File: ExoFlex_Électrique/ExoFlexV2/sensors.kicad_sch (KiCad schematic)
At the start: 38 parts, among them J10 Screw_Terminal_01x02, J11 Screw_Terminal_01x02, J12 Screw_Terminal_01x02, J13 Screw_Terminal_01x02, J14 Screw_Terminal_01x02, J15 Screw_Terminal_01x02, J16 Screw_Terminal_01x02, J17 Screw_Terminal_5V, J18 Screw_Terminal_01x02, J19 Screw_Terminal_GND, J8 Screw_Terminal_01x02, J9 Screw_Terminal_01x02, Q1 S8550, Q2 S8550, Q3 S8550, U10 Switch(5A), U11 Switch(5A), U12 Switch(5A), U5 HX711, U6 HX711, U7 HX711, U8 MPU6050_acc_gyro, U9 MPU6050_acc_gyro

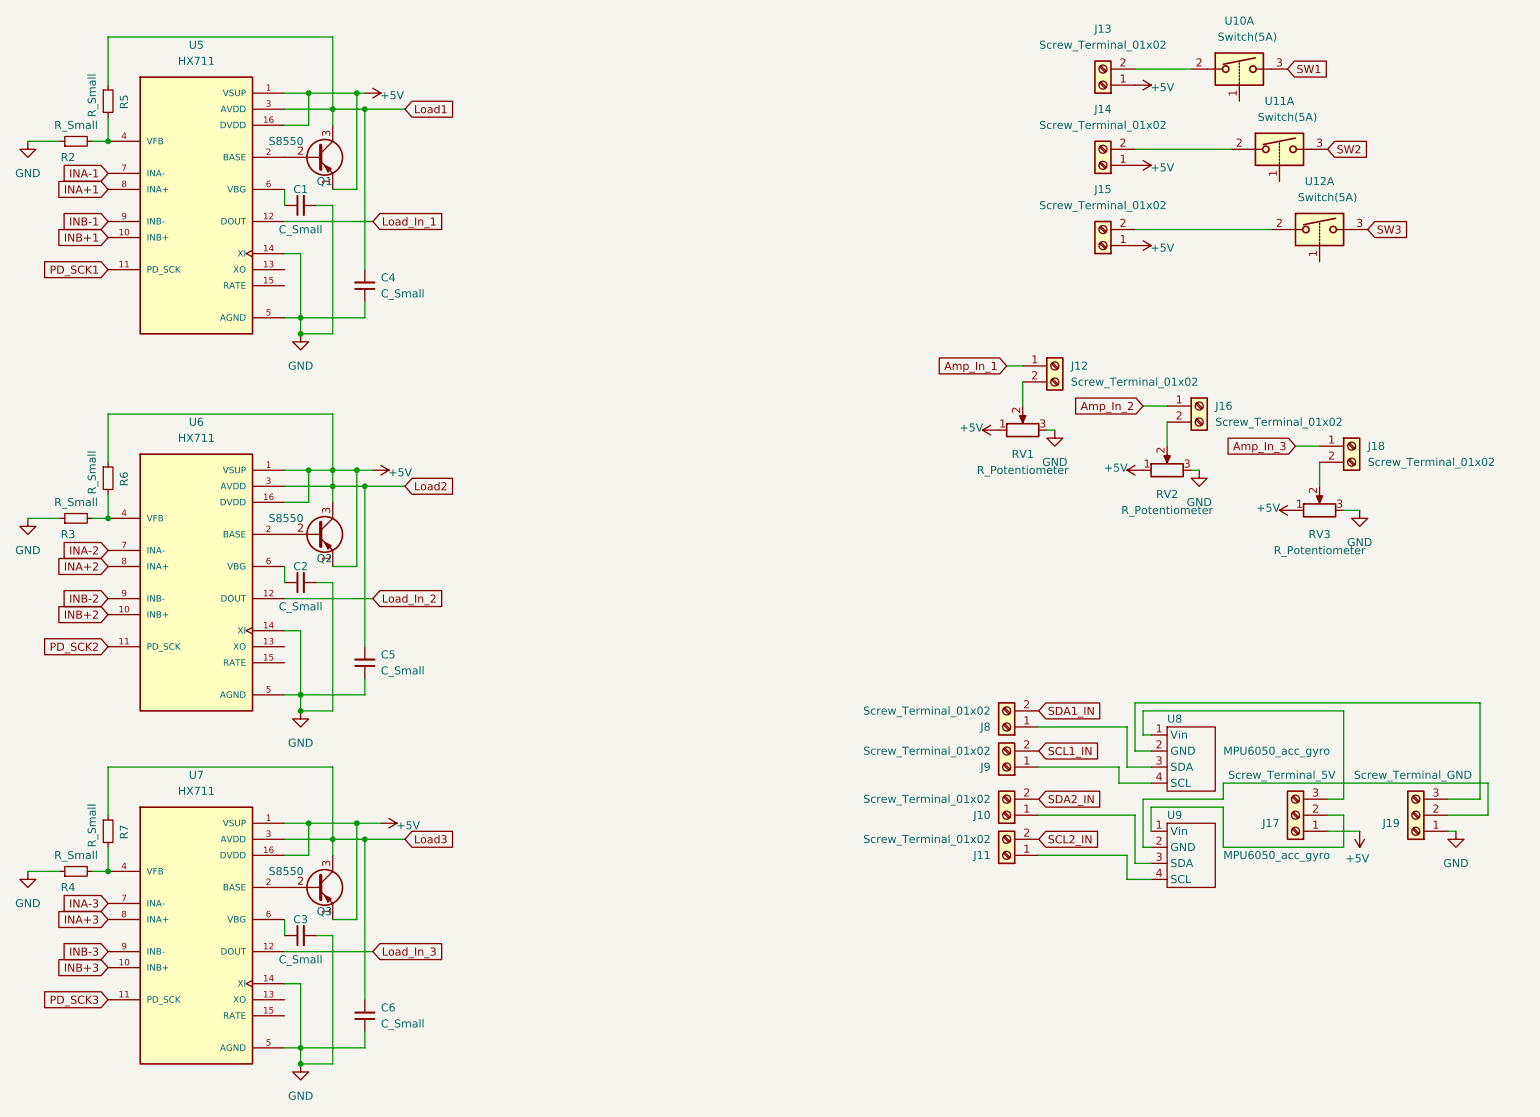
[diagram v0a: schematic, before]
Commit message: Modification du schéma électrique en enlevant les cellules de charge et les cicuits de potentio
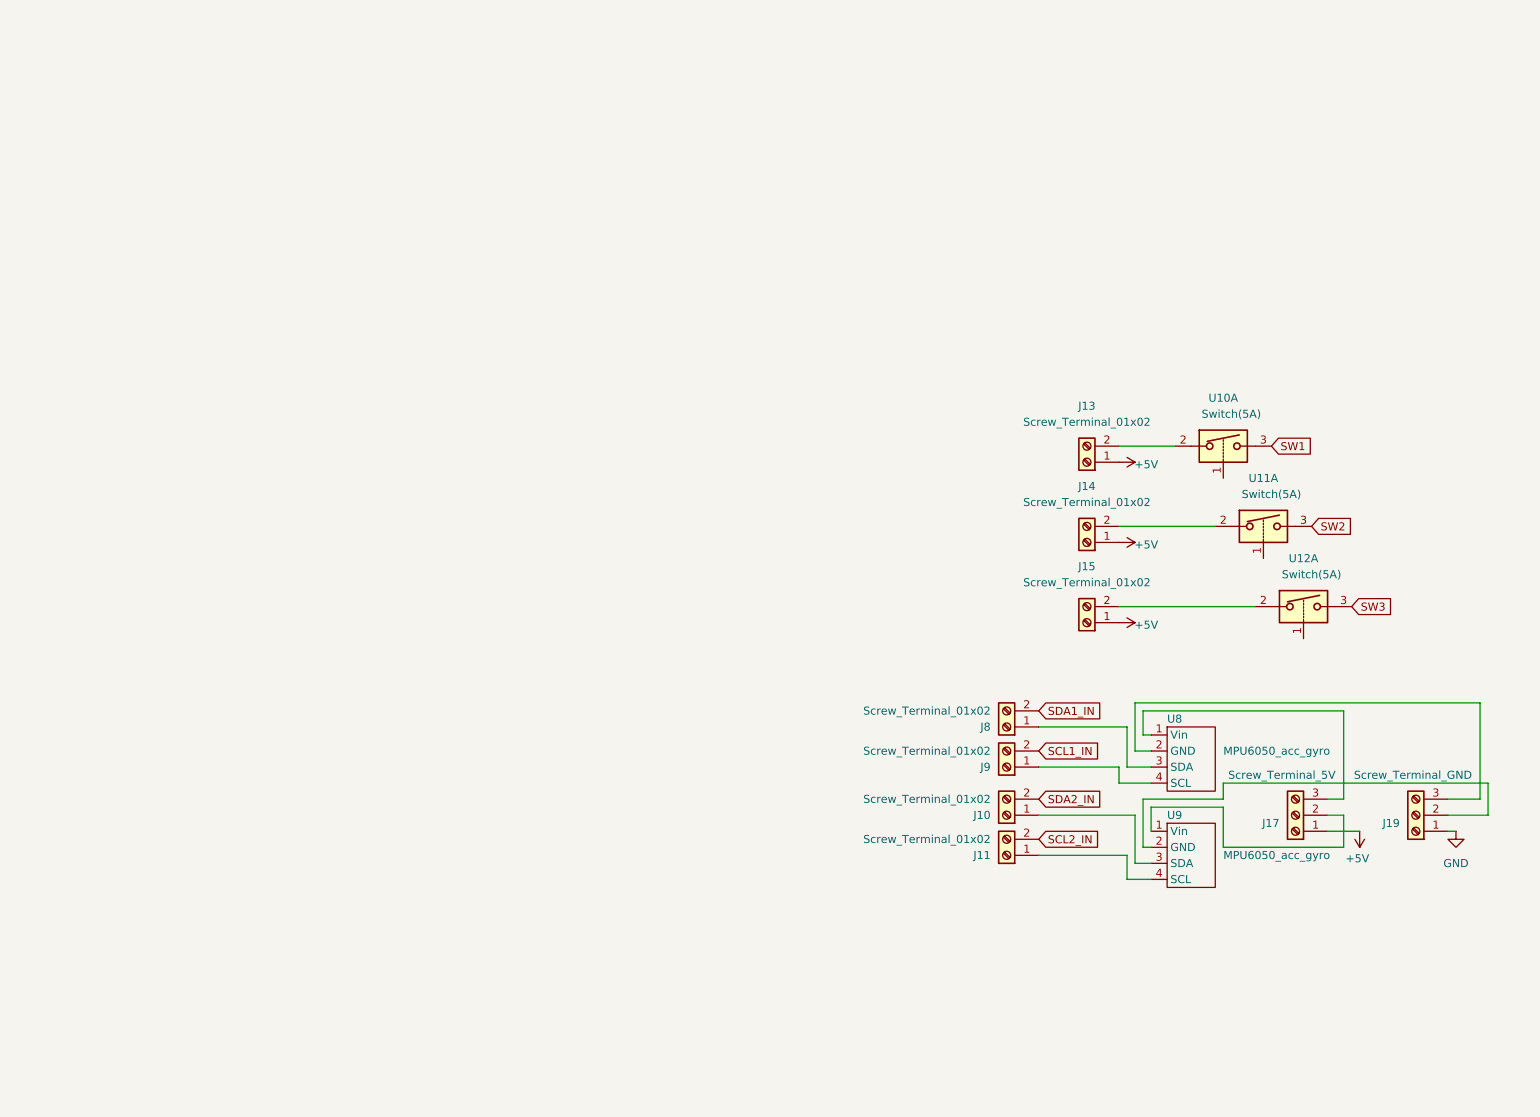
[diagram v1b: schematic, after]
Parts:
- removed C1, C2, C3, C4, C5, C6: C_Small, symbol Device:C_Small
- removed J12, J16, J18: Screw_Terminal_01x02, symbol Connector:Screw_Terminal_01x02
- removed Q1, Q2, Q3: S8550, Package_TO_SOT_THT:TO-92_Inline, symbol Transistor_BJT:S8550
- removed R2, R3, R4, R5, R6, R7: R_Small, symbol Device:R_Small
- removed RV1, RV2, RV3: R_Potentiometer, symbol Device:R_Potentiometer
- removed U5, U6, U7: HX711, SOP127P600X180-16N, symbol Sensor_library:HX711
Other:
- moved on the sheet: J13, J14, J15, U10A, U11A, U12A
